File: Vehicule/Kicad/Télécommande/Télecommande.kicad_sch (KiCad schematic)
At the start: 5 parts, among them J1 Conn_01x02_Socket, U1 ESP32-C3_SUPERMINI

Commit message: Transfert du SUPERMINI (composant et empreintes) dans les librairies locales (Anumby et Empreintes) Renommer Empreintes -> Anumby
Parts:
- J1: footprint Empreintes:CONN-2-PINS -> Anumby:CONN-2-PINS
- R1: footprint Empreintes:Joystick -> Anumby:Joystick
- U1: footprint PCM_Espressif:ESP32-C3-SUPERMINI -> Anumby:ESP32-C3-SUPERMINI
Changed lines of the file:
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@@
 			)
 		)
-		(property "Footprint" "PCM_Espressif:ESP32-C3-SUPERMINI"
+		(property "Footprint" "Anumby:ESP32-C3-SUPERMINI"
 			(at 81.28 72.39 0)
 			(effects
@@
 			)
 		)
-		(property "Footprint" "Empreintes:CONN-2-PINS"
+		(property "Footprint" "Anumby:CONN-2-PINS"
 			(at 110.49 68.58 0)
 			(effects
@@
 			)
 		)
-		(property "Footprint" "Empreintes:Joystick"
+		(property "Footprint" "Anumby:Joystick"
 			(at 115.57 81.28 0)
 			(effects

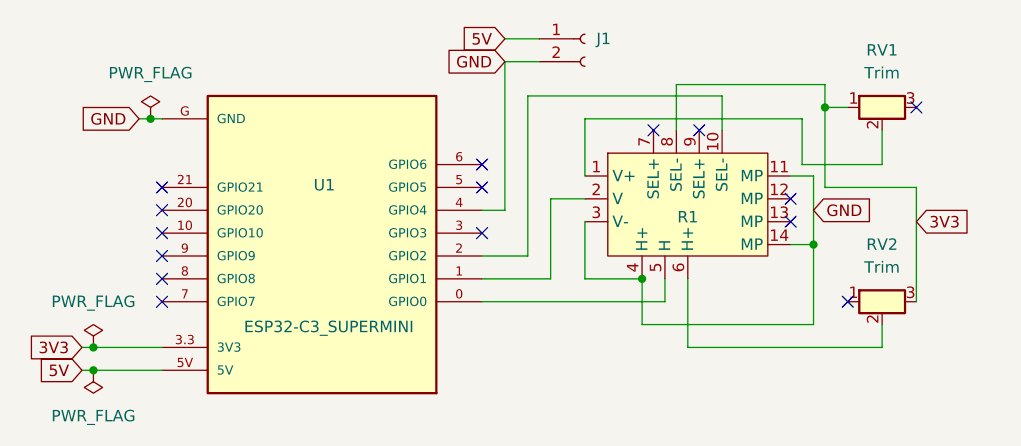
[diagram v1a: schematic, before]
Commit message: TAjouter la couche de masse pour la télécommande
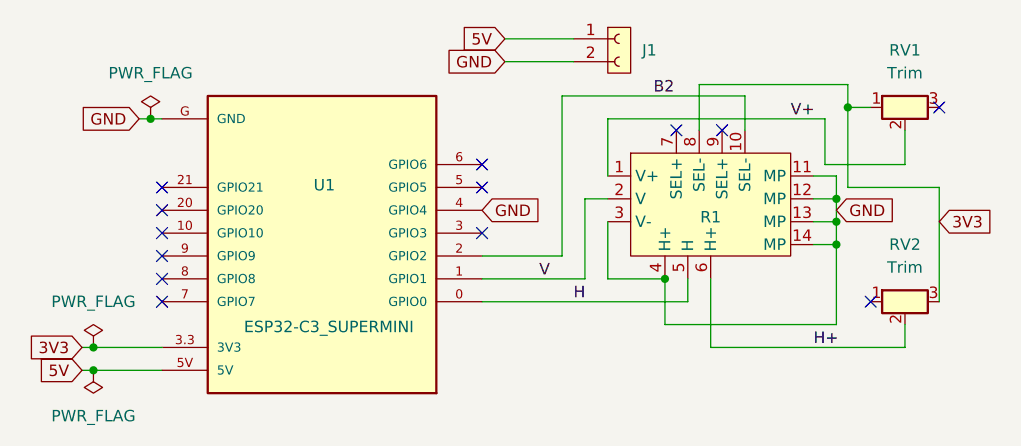
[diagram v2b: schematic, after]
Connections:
- net GND: now also R1.12 (MP), R1.13 (MP)
- net H+: now reaches R1.6 (H+), RV2.2
- net H: now reaches R1.5 (H), U1.0 (GPIO0)
- net V: now reaches R1.2 (V), U1.1 (GPIO1)
- net B2: now reaches R1.10 (SEL-), U1.2 (GPIO2)
- net V+: now reaches R1.1 (V+), RV1.2
- no-connect marks 15 -> 13
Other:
- moved on the sheet: R1, RV1, RV2

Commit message: Ajout de la couche de masse pour Robot Ajout d'un connecteur 1 pin Mise à jour de tous les PCB et les Schémas
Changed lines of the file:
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@@
-	)
-	(symbol
-		(lib_id "Anumby:Conn_01x02_Socket")
-		(at 114.3 68.58 0)
-		(unit 1)
-		(exclude_from_sim no)
-		(in_bom yes)
-		(on_board yes)
-		(dnp no)
-		(fields_autoplaced yes)
-		(property "Reference" "J1"
-			(at 116.84 69.8499 0)
-			(effects
-				(font
-					(size 1.27 1.27)
-				)
-				(justify left)
-			)
-		)
-		(property "Value" "Conn_01x02_Socket"
-			(at 100.838 76.962 0)
-			(effects
-				(font
-					(size 1.27 1.27)
-				)
-				(justify left)
-				(hide yes)
-			)
-		)
-		(property "Footprint" "Anumby:CONN-2-PINS"
-			(at 109.22 62.738 0)
-			(effects
-				(font
-					(size 1.27 1.27)
-				)
-				(hide yes)
-			)
-		)
-		(property "Datasheet" ""
-			(at 114.3 68.58 0)
-			(effects
-				(font
-					(size 1.27 1.27)
-				)
-				(hide yes)
-			)
-		)
-		(property "Description" "Generic connector, single row, 01x02, script generated"
-			(at 113.538 65.024 0)
-			(effects
-				(font
-					(size 1.27 1.27)
-				)
-				(hide yes)
-			)
-		)
-		(pin "1"
-		)
-		(pin "2"
-		)
-		(instances
-			(project ""
-				(path "/53aa335e-ed34-4147-b76c-4ae08837133c"
-					(reference "J1")
-					(unit 1)
-				)
-			)
-		)
 	)
 	(symbol
@@
 					(unit 1)
 				)
+			)
+		)
+	)
+	(symbol
+		(lib_id "Anumby:Conn_01x02_Socket")
+		(at 114.3 68.58 0)
+		(unit 1)
+		(exclude_from_sim no)
+		(in_bom yes)
+		(on_board yes)
+		(dnp no)
+		(fields_autoplaced yes)
+		(property "Reference" "J1"
+			(at 118.11 68.5799 0)
+			(effects
+				(font
+					(size 1.27 1.27)
+				)
+				(justify left)
+			)
+		)
+		(property "Value" "Conn_01x02_Socket"
+			(at 118.11 71.1199 0)
+			(effects
+				(font
+					(size 1.27 1.27)
+				)
+				(justify left)
+			)
+		)
+		(property "Footprint" "Anumby:CONN-2-PINS"
+			(at 114.046 65.786 0)
+			(effects
+				(font
+					(size 1.27 1.27)
+				)
+				(hide yes)
+			)
+		)
+		(property "Datasheet" ""
+			(at 114.3 68.58 0)
+			(effects
+				(font
+					(size 1.27 1.27)
+				)
+				(hide yes)
+			)
+		)
+		(property "Description" ""
+			(at 115.062 62.992 0)
+			(effects
+				(font
+					(size 1.27 1.27)
+				)
+				(hide yes)
+			)
+		)
+		(pin "1"
+		)
+		(pin "2"
+		)
+		(instances
+			(project ""
+				(path "/53aa335e-ed34-4147-b76c-4ae08837133c"
+					(reference "J1")
+					(unit 1)
+				)

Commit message: Ajout de logo Anumby pour PCB Mise à jour des empreintes, des connecteurs des librairies
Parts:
- removed J1: Conn_01x02_Socket, Anumby:CONN-2-PINS, symbol Anumby:Conn_01x02_Socket
- added J1: Conn_01x02_Socket_H, Connector_JST:JST_PH_S2B-PH-K_1x02_P2.00mm_Horizontal, symbol Anumby:Conn_01x02_Socket_H
- R1: footprint Anumby:Joystick -> Anumby:JOYSTICK_MODEL_802
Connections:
- net 5V: now also J1.1 (Pin_1)
- net GND: now also J1.2 (Pin_2)
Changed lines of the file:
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@@
-	)
-	(symbol
-		(lib_id "Anumby:Conn_01x02_Socket")
-		(at 114.3 68.58 0)
-		(unit 1)
-		(exclude_from_sim no)
-		(in_bom yes)
-		(on_board yes)
-		(dnp no)
-		(fields_autoplaced yes)
-		(property "Reference" "J1"
-			(at 118.11 68.5799 0)
-			(effects
-				(font
-					(size 1.27 1.27)
-				)
-				(justify left)
-			)
-		)
-		(property "Value" "Conn_01x02_Socket"
-			(at 118.11 71.1199 0)
-			(effects
-				(font
-					(size 1.27 1.27)
-				)
-				(justify left)
-			)
-		)
-		(property "Footprint" "Anumby:CONN-2-PINS"
-			(at 114.046 65.786 0)
-			(effects
-				(font
-					(size 1.27 1.27)
-				)
-				(hide yes)
-			)
-		)
-		(property "Datasheet" ""
-			(at 114.3 68.58 0)
-			(effects
-				(font
-					(size 1.27 1.27)
-				)
-				(hide yes)
-			)
-		)
-		(property "Description" ""
-			(at 115.062 62.992 0)
-			(effects
-				(font
-					(size 1.27 1.27)
-				)
-				(hide yes)
-			)
-		)
-		(pin "1"
-		)
-		(pin "2"
-		)
-		(instances
-			(project ""
-				(path "/53aa335e-ed34-4147-b76c-4ae08837133c"
-					(reference "J1")
-					(unit 1)
-				)
-			)
-		)
 	)
 	(symbol
@@
 			)
 		)
-		(property "Footprint" "Anumby:Joystick"
+		(property "Footprint" "Anumby:JOYSTICK_MODEL_802"
 			(at 122.682 72.136 0)
 			(effects
@@
 					(unit 1)
 				)
+			)
+		)
+	)
+	(symbol
+		(lib_id "Anumby:Conn_01x02_Socket_H")
+		(at 114.3 68.58 0)
+		(unit 1)
+		(exclude_from_sim no)
+		(in_bom yes)
+		(on_board yes)
+		(dnp no)
+		(fields_autoplaced yes)
+		(property "Reference" "J1"
+			(at 118.11 68.5799 0)
+			(effects
+				(font
+					(size 1.27 1.27)
+				)
+				(justify left)
+			)
+		)
+		(property "Value" "Conn_01x02_Socket_H"
+			(at 118.11 71.1199 0)
+			(effects
+				(font
+					(size 1.27 1.27)
+				)
+				(justify left)
+			)
+		)
+		(property "Footprint" "Connector_JST:JST_PH_S2B-PH-K_1x02_P2.00mm_Horizontal"
+			(at 114.046 65.786 0)
+			(effects
+				(font
+					(size 1.27 1.27)
+				)
+				(hide yes)
+			)
+		)
+		(property "Datasheet" ""
+			(at 114.3 68.58 0)
+			(effects
+				(font
+					(size 1.27 1.27)
+				)
+				(hide yes)
+			)
+		)
+		(property "Description" ""
+			(at 115.062 62.992 0)
+			(effects
+				(font
+					(size 1.27 1.27)
+				)
+				(hide yes)
+			)
+		)
+		(pin "2"
+		)
+		(pin "1"
+		)
+		(instances
+			(project ""
+				(path "/53aa335e-ed34-4147-b76c-4ae08837133c"
+					(reference "J1")
+					(unit 1)
+				)
